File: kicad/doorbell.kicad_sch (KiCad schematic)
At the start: 106 parts, among them J1 USB-C (USB4105), J2 WF26 bus, J3 USB-JST, K1 GAQW212GS, K2 GAQY212GS, K3 GAQY412EH, K4 GAQY412EH, K5 G6K-2F-Y DC12, Q3 AO3400A, Q4 AO3400A, SW1 BOOT, SW2 EN, SW3 Tueroeffner (door release), SW4 Sprechen/Hoeren (talk), U1 ESP32-S3-WROOM-1U-N16R8, U2 SGM2212-3.3, U3 ES8311, U4 LP5907MFX-3.3

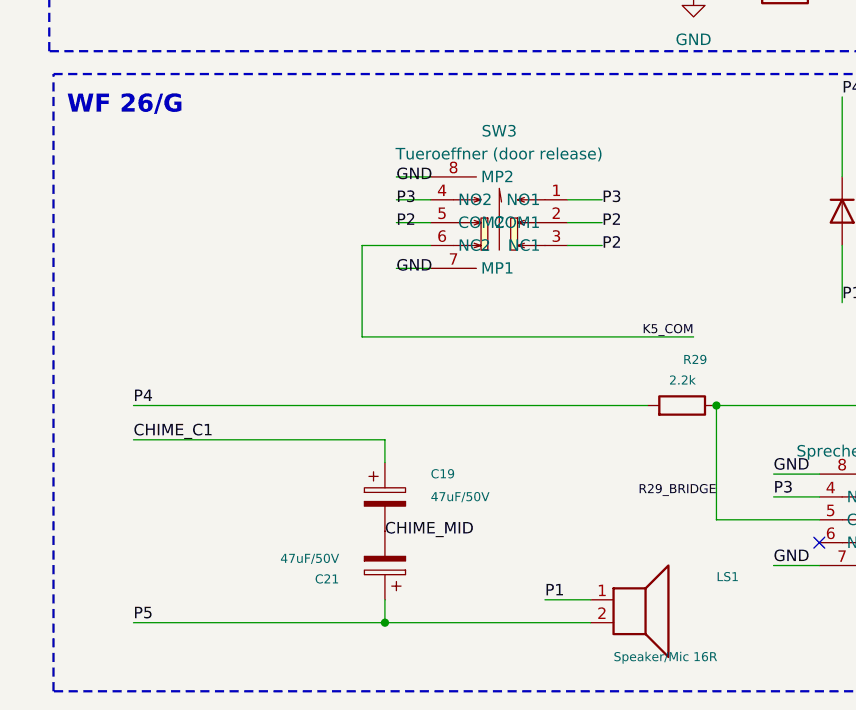
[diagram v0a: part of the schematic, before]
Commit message: Add selectable chime charge bleed
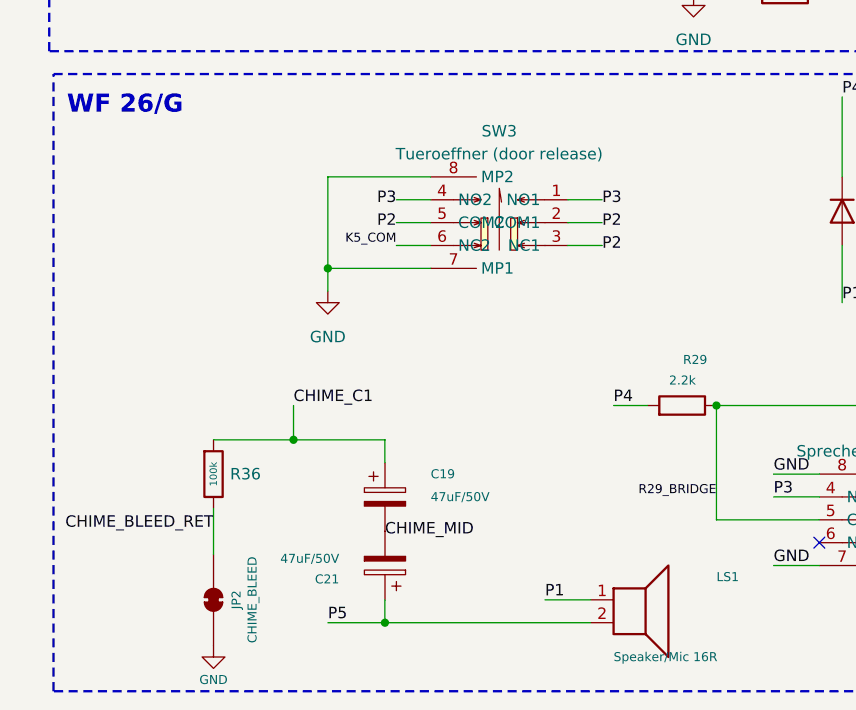
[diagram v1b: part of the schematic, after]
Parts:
- added JP2: CHIME_BLEED, Jumper:SolderJumper-2_P1.3mm_Bridged_RoundedPad1.0x1.5mm, symbol Jumper:SolderJumper_2_Bridged
- added R36: 100k, PCM_JLCPCB:R_0603, symbol PCM_JLCPCB-Resistors:0603,100kΩ
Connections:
- net CHIME_C1: now also R36.1
- net GND: now also JP2.1 (A)
- new net CHIME_BLEED_RET: JP2.2 (B), R36.2

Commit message: Use revision-neutral project naming
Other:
- title: Doorbell controller (Klingel V4) -> Doorbell controller
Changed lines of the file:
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@@
 	(paper "A3")
 	(title_block
-		(title "Doorbell controller (Klingel V4)")
+		(title "Doorbell controller")
 		(date "2026-07-02")
 		(rev "V4.2")

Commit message: Move status LED and restore handset after gong
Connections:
- net STATUS_LED: now also U1.22 (IO14); no longer U1.15 (IO3)
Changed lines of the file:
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@@
 	)
 	(no_connect
-		(at 130.81 67.31)
-	)
-	(no_connect
 		(at 161.29 26.67)
 	)
@@
 	)
 	(no_connect
+		(at 130.81 39.37)
+	)
+	(no_connect
 		(at 130.81 72.39)
 	)
@@
 	(wire
 		(pts
-			(xy 123.19 39.37) (xy 130.81 39.37)
-		)
-		(stroke
-			(width 0)
-			(type default)
-		)
-	)
-	(wire
-		(pts
 			(xy 228.6 213.36) (xy 228.6 217.17)
 		)
@@
 	(wire
 		(pts
+			(xy 123.19 67.31) (xy 130.81 67.31)
+		)
+		(stroke
+			(width 0)
+			(type default)
+		)
+	)
+	(wire
+		(pts
 			(xy 320.04 95.25) (xy 320.04 102.87)
 		)
@@
 		)
 	)
+	(label "STATUS_LED"
+		(at 123.19 67.31 180)
+		(effects
+			(font
+				(size 1 1)
+			)
+			(justify right bottom)
+		)
+	)
 	(label "P2"
 		(at 52.07 227.33 180)
@@
 		)
 	)
-	(label "STATUS_LED"
-		(at 123.19 39.37 180)
-		(effects
-			(font
-				(size 1 1)
-			)
-			(justify right bottom)
-		)
-	)
 	(label "+3V3"
 		(at 232.41 148.59 0)
@@
 			)
 		)
-		(property "Description" "Status LED (IO3, active-low)"
+		(property "Description" "Status LED (IO14, active-low)"
 			(at 237.49 73.66 0)
 			(hide yes)

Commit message: Add K5-gated P4 isolation
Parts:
- removed C25, C26: 22uF, PCM_JLCPCB:C_1206, symbol PCM_JLCPCB-Capacitors:1206,22uF,(2)
- removed JP1: SolderJumper_2_Bridged, Jumper:SolderJumper-2_P1.3mm_Bridged_RoundedPad1.0x1.5mm, symbol Jumper:SolderJumper_2_Bridged
- removed R35: 1kΩ, PCM_JLCPCB:R_1206, symbol PCM_JLCPCB-Resistors:1206,1kΩ
- added JP3: K6_BYPASS, Jumper:SolderJumper-2_P1.3mm_Open_RoundedPad1.0x1.5mm, symbol Jumper:SolderJumper_2_Open
- added K6: GAQY412EH, gaqy412eh:SMD-4_L4.8-W6.4-P2.54-LS9.6-BL, symbol gaqy412eh:GAQY412EH
- added R12, R35: 10k, PCM_JLCPCB:R_0402, symbol PCM_JLCPCB-Resistors:0402,10kΩ
- added R34: 220, PCM_JLCPCB:R_0603, symbol PCM_JLCPCB-Resistors:0603,220Ω
- R28: renamed from R34; value 1.2kΩ -> 2.2kΩ; footprint PCM_JLCPCB:R_1206 -> PCM_JLCPCB:R_0603; LCSC C17891 -> C4190; MPN 1206W4F1201T5E -> 0603WAF2201T5E
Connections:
- net HS_FILT is gone; now on net TX_OUT: R28.1
- net +3V3: now also R35.1
- net GND: now also K5.6, R12.2
- net P4: now also JP3.2 (B), K6.4; no longer D1.1 (K), K5.1, K5.4, R29.1
- net TALK_BRIDGE: now also C14.2
- net TX_OUT: no longer C14.2
- net K5_SENSE: now reaches K5.5
- net K5_SENSE: now also U1.4 (IO4), K6.2, R35.2
- net ISO_REQ: now reaches U1.25 (IO48)
- net ISO_REQ: now also R12.1, R34.2
- new net K5_LATCH: D1.1 (K), JP3.1 (A), K5.1, K5.4, K6.3, R29.1
- new net K6_LED: K6.1, R34.1
- no-connect marks 28 -> 24
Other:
- note added: "ISOLATE P4 (K6, NC SRR)"
- note added: "TALK (K1, dual NO SSR) ch1: P2 <-> TALK_BRIDGE; TALK_BRIDGE -> R28 2.2k -> TX_OUT; ch2: TX_OUT <-> P3; codec TX -> R26/C14 -> TALK_BRIDGE"
- note removed: "TALK (K1, dual NO SSR) ch1: P2 -> Ra/Cf/Rb LPF -> TX_OUT (the 2.2k talk handshake, gong-stripped); ch2: TX_OUT <-> P3 (handshake + codec TX via C14); cut JP1 = plain 2.2k strap (V4.1 fallback)"
- moved on the sheet: C18, C20, D11, K3, K4, Q3, Q4, R17, R21, R25, R28, R5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

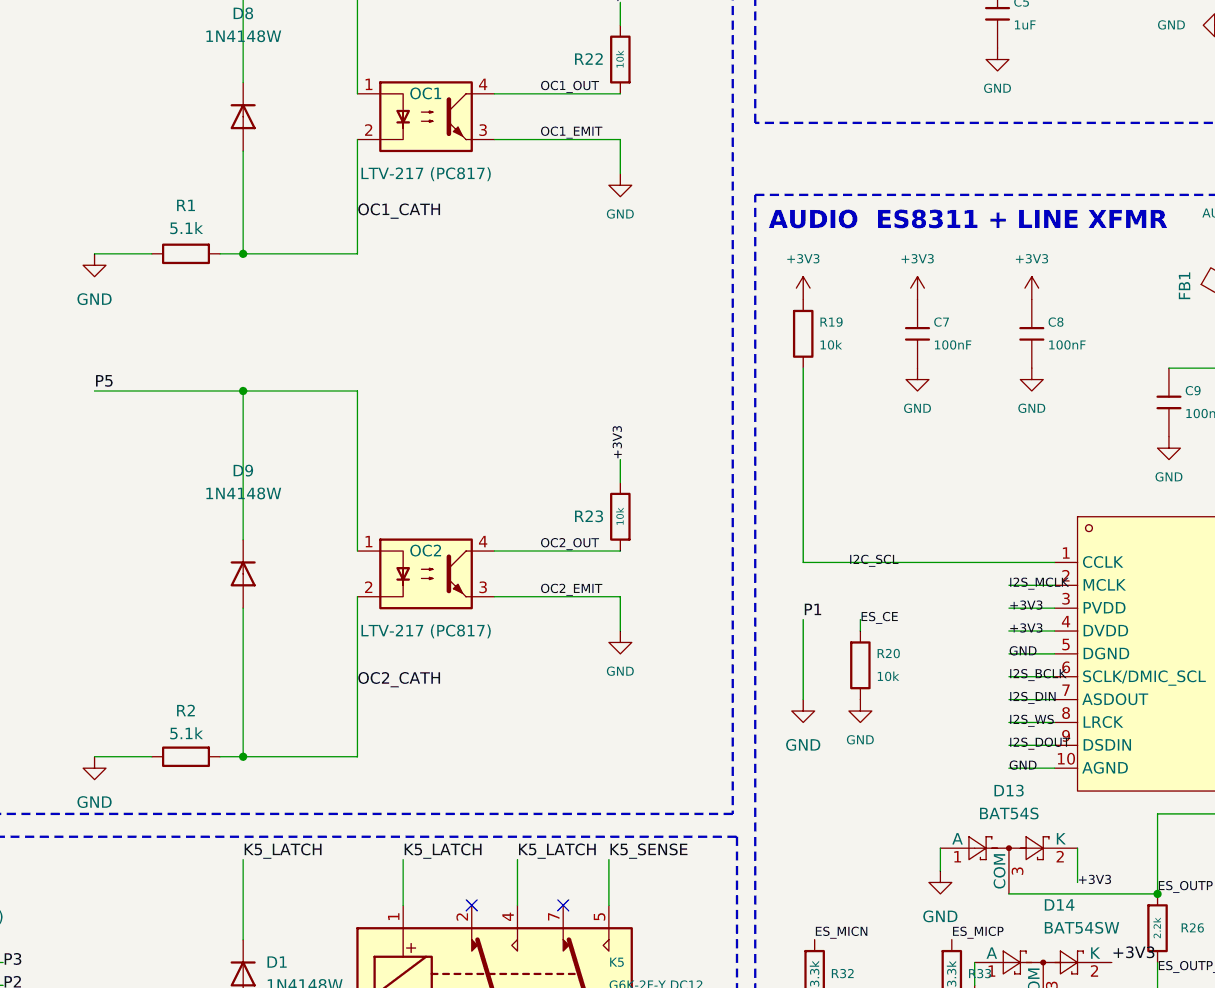
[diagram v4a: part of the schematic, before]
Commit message: hardware: update ring sensing and assembly outputs
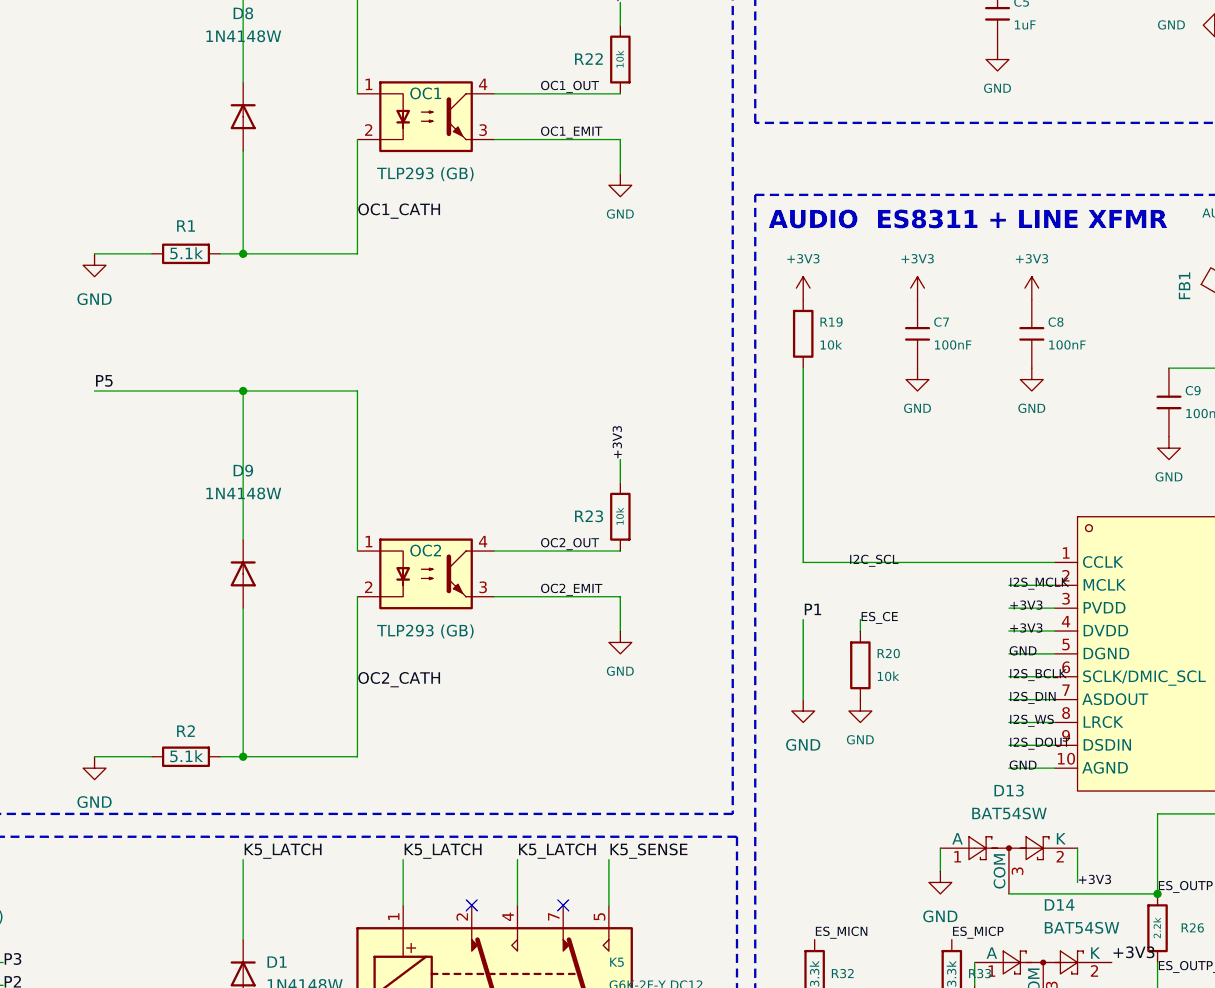
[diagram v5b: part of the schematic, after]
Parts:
- D13: value BAT54S -> BAT54SW; footprint Package_TO_SOT_SMD:SOT-23 -> Package_TO_SOT_SMD:SOT-323_SC-70; symbol Diode:BAT54S -> Diode:BAT54SW; LCSC C7420333 -> C22466373; MPN BAT54S -> BAT54SW
- OC1, OC2: value LTV-217 (PC817) -> TLP293 (GB); footprint PCM_JLCPCB:SOP-4_4.4x2.6mm_P1.27mm -> tlp293:SOP-4_L4.4-W2.8-P1.27-LS7.0-BR; symbol PCM_JLCPCB-Optocouplers:LTV-217-B-G -> tlp293:TLP293; LCSC C115450 -> C77656; MPN LTV-217-B-G -> TLP293(GB-TPL,E; Manufacturer (none) -> Toshiba

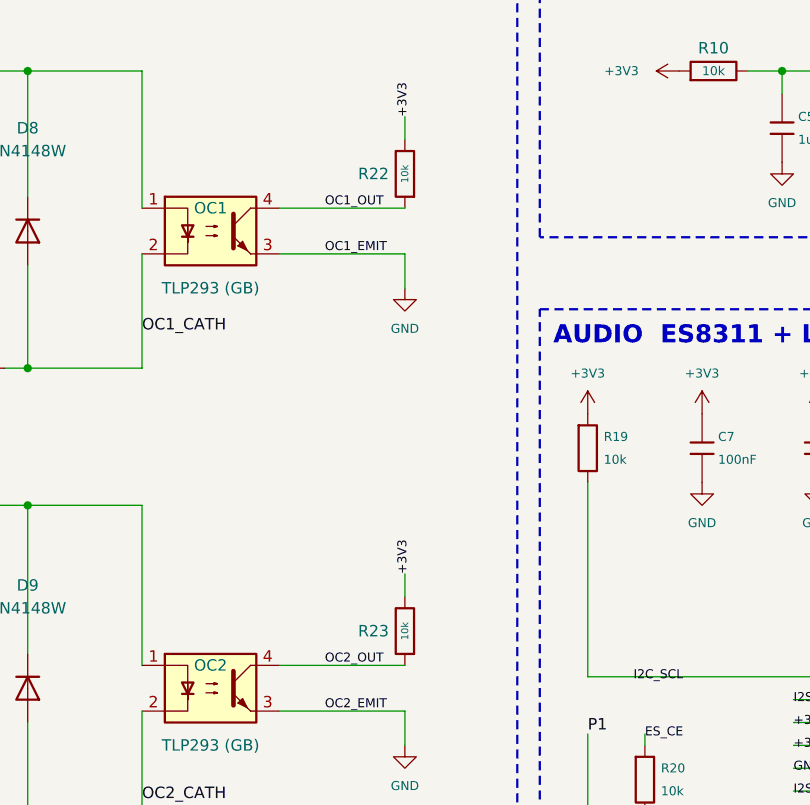
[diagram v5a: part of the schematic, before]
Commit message: hardware: close optocoupler sensing margins
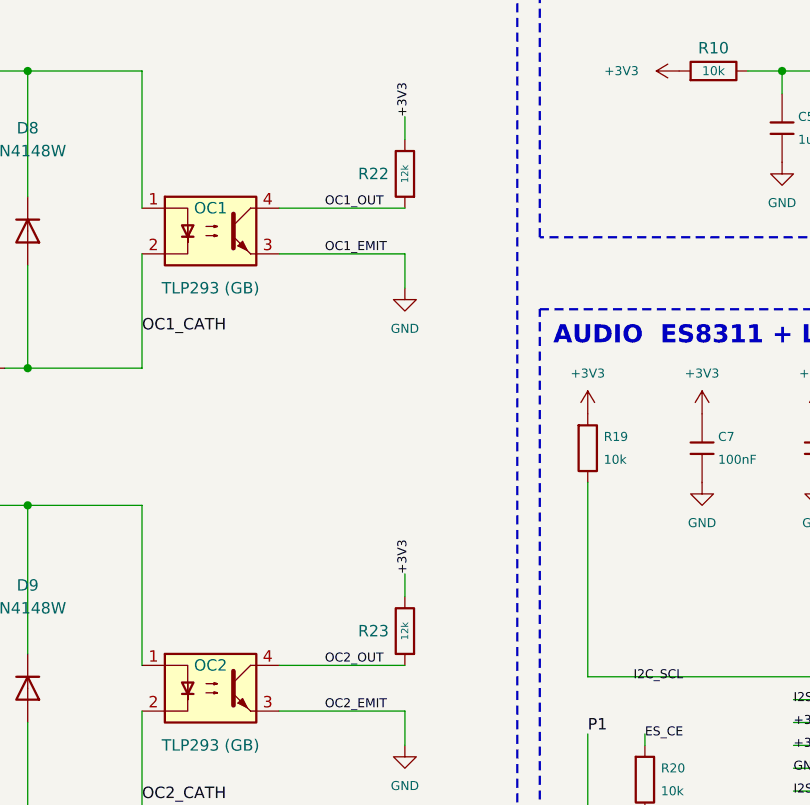
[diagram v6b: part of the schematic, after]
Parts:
- R22, R23: value 10k -> 12k; symbol PCM_JLCPCB-Resistors:0402,10kΩ -> PCM_JLCPCB-Resistors:0402,12kΩ; LCSC C25744 -> C25752; MPN 0402WGF1002TCE -> 0402WGF1202TCE

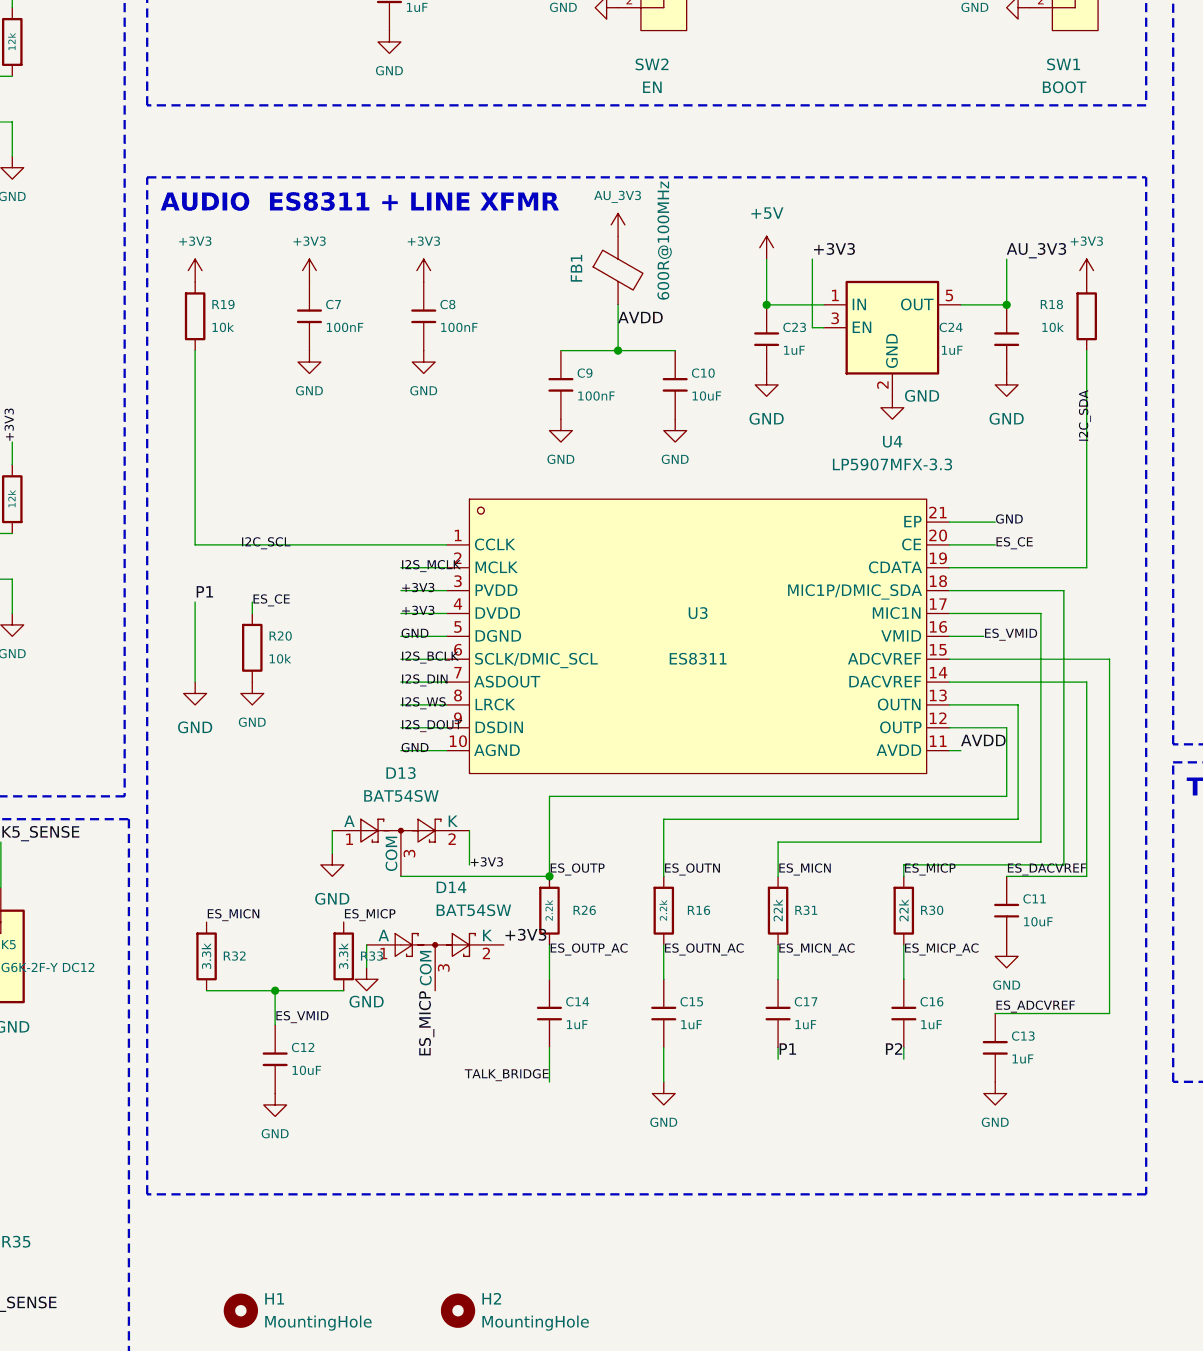
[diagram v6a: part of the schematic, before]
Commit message: hardware: qualify ES8311 clamp network
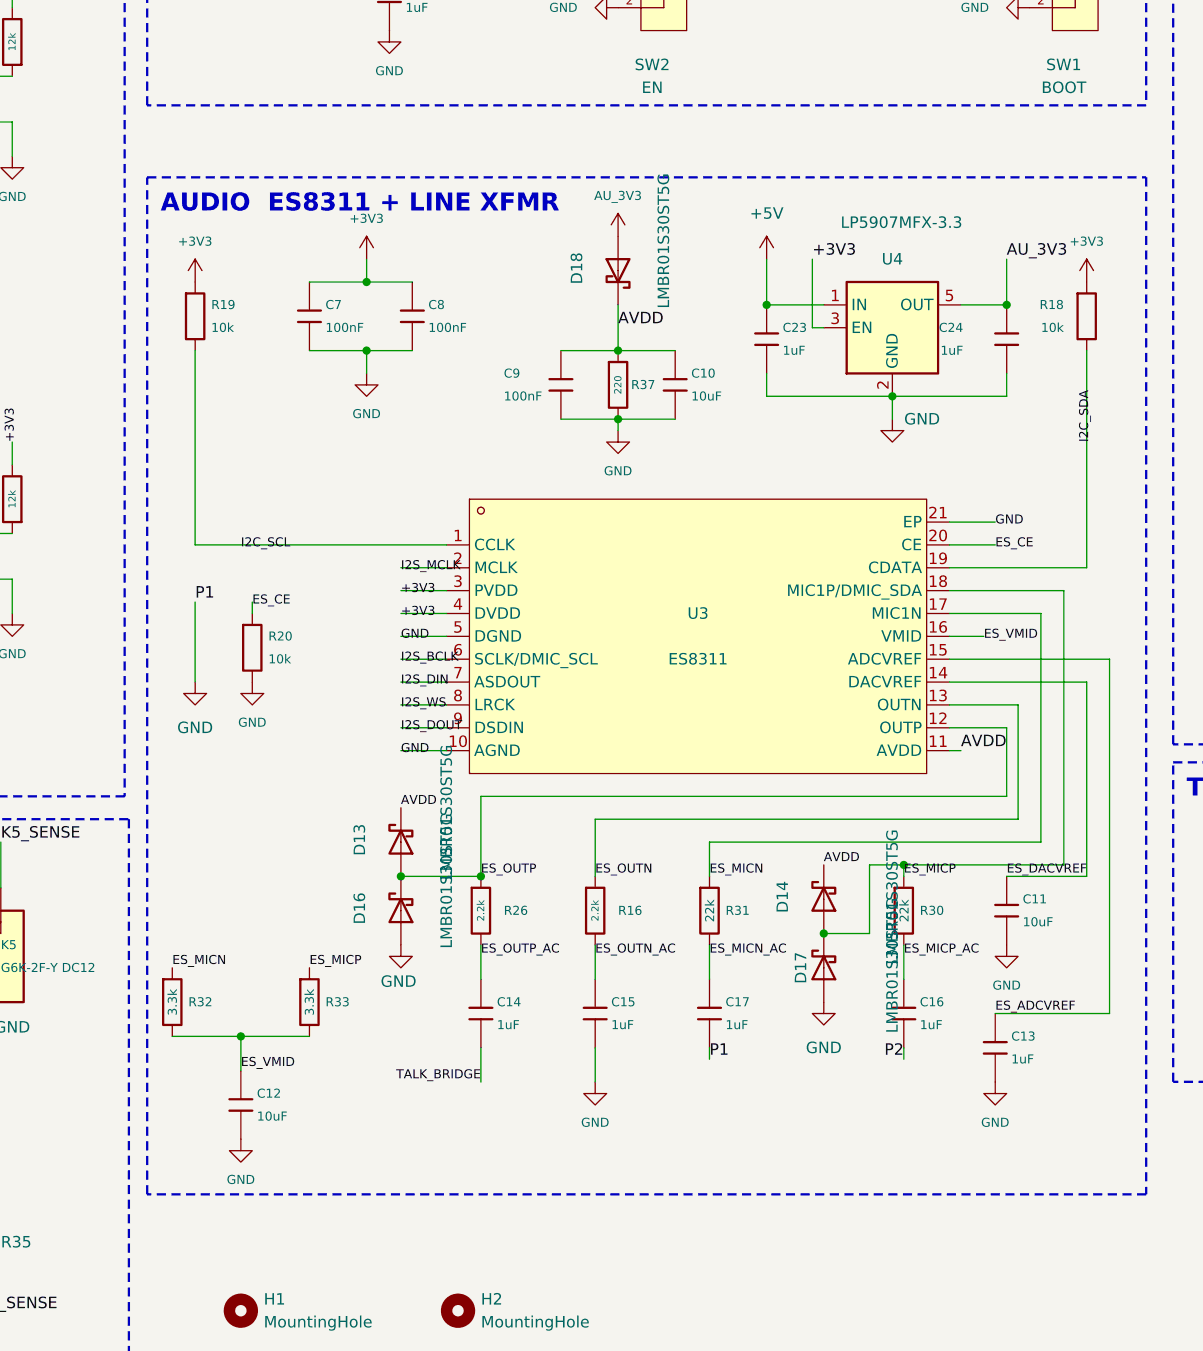
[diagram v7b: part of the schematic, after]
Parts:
- added D16, D17: LMBR01S30ST5G, lmbr01s30st5g:X3-DFN0603-2_L0.6-W0.3-RD, symbol PCM_JLCPCB-Diodes:Schottky,SS14
- added R37: 220, Resistor_SMD:R_0603_1608Metric, symbol PCM_JLCPCB-Resistors:0603,220Ω
- D13, D14: value BAT54SW -> LMBR01S30ST5G; footprint Package_TO_SOT_SMD:SOT-323_SC-70 -> lmbr01s30st5g:X3-DFN0603-2_L0.6-W0.3-RD; symbol Diode:BAT54SW -> PCM_JLCPCB-Diodes:Schottky,SS14; LCSC C22466373 -> C383224; MPN BAT54SW -> LMBR01S30ST5G; Manufacturer hongjiacheng -> Leshan Radio Company (LRC)
- D18: renamed from FB1; value 600R@100MHz -> LMBR01S30ST5G; footprint Inductor_SMD:L_0603_1608Metric -> lmbr01s30st5g:X3-DFN0603-2_L0.6-W0.3-RD; symbol Device:FerriteBead -> PCM_JLCPCB-Diodes:Schottky,SS14; LCSC C1002 -> C383224; MPN GZ1608D601TF -> LMBR01S30ST5G; Manufacturer Sunlord -> Leshan Radio Company (LRC)
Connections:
- net +3V3: no longer D13.2 (K), D14.2 (K)
- net AU_3V3: now also D18.2; no longer D18.1
- net AVDD: now also D13.1, D14.1, D18.1, R37.1; no longer D18.2
- net ES_MICP: now also D14.2, D17.1; no longer D14.3 (COM)
- net ES_OUTP: now also D13.2, D16.1; no longer D13.3 (COM)
- net GND: now also D16.2, D17.2, R37.2; no longer D13.1 (A), D14.1 (A)
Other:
- moved on the sheet: C12, C14, C15, C17, C8, R16, R26, R31, R32, R33
